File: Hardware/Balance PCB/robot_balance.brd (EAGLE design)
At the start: 100 x 50 mm, 47 parts, among them Q1 16Mhz

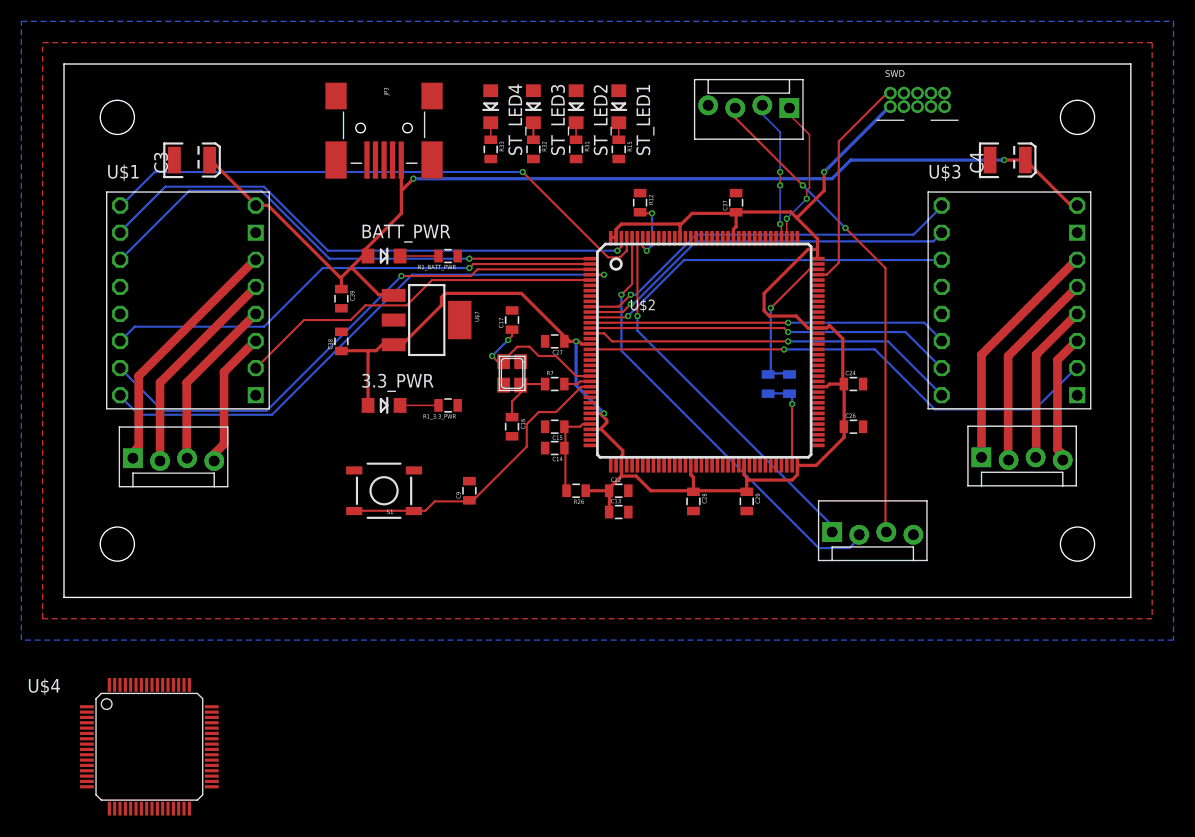
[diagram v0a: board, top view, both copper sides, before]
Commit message: Replaced 144 pin Balancing MCU with smaller 64 pin version and added a .gitignore file
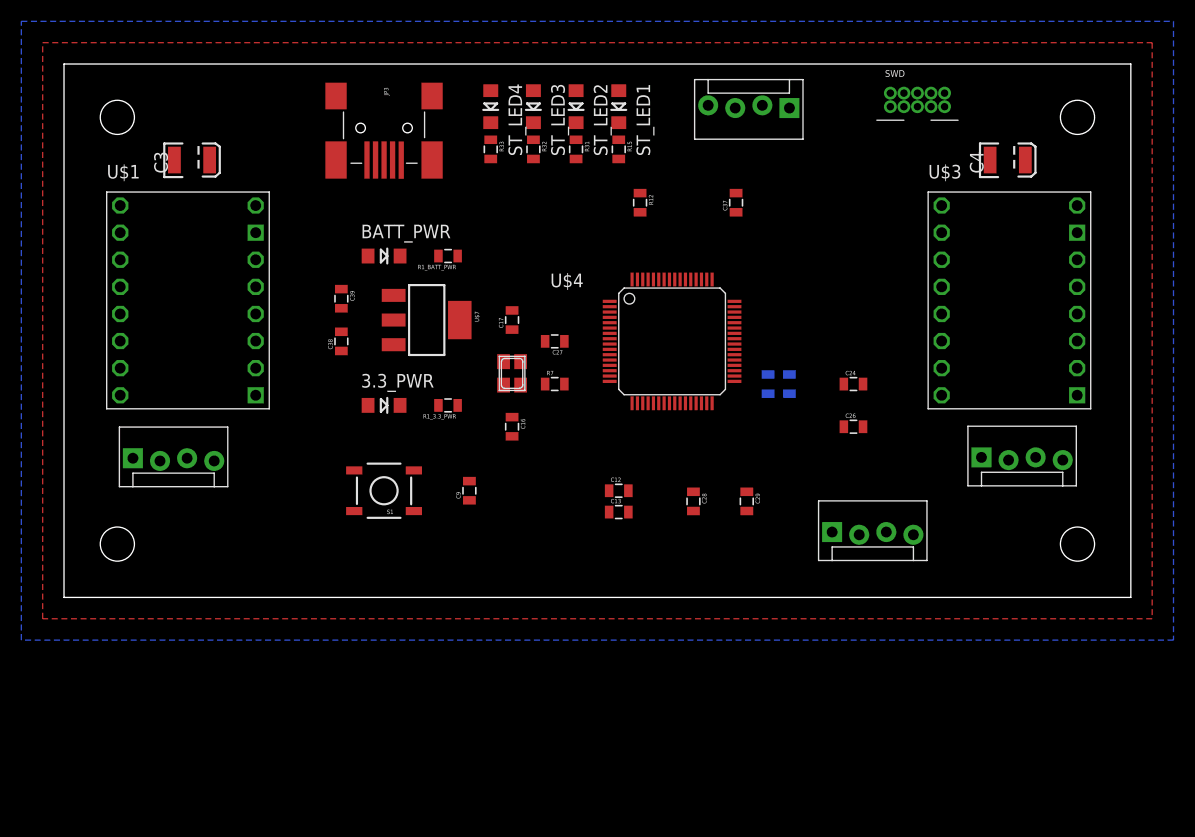
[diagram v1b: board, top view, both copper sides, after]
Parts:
- removed C14: 0.1uF, SparkFun-Capacitors:0805
- removed C15: 1uF, SparkFun-Capacitors:0805
- removed R26: 47, SparkFun-Passives:0805
- removed U$2: STM32F407ZG, CAMERA:LQFP-144-20X20MM
- moved U$4 62.0 mm to (57.0, 24.0)
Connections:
- removed net N$10: C9.1, S1.1, S1.2, U$2.25
- removed net N$11: R12.2, U$2.138
- removed net N$14: C14.1, C15.1, R26.2, U$2.32
- removed net N$15: C17.1, Q1.3, U$2.23
- removed net N$22: R7.2, U$2.24
- removed net N$42: ST_LED1.A, U$2.127
- removed net N$44: ST_LED2.A, U$2.128
- removed net N$46: ST_LED3.A, U$2.129
- removed net N$48: ST_LED4.A, U$2.132
- removed net NRST: U$4.7
- removed net VCAP_1: U$4.31
- removed net VCAP_2: U$4.47
- removed net VDDA: U$4.13
- removed net VDD_1: U$4.32
- removed net VDD_2: U$4.48
- removed net VDD_3: U$4.64
- removed net VDD_4: U$4.19
- removed net VSSA: U$4.12
- removed net VSS_3: U$4.63
- removed net VSS_4: U$4.18
- new net !RST: C9.1, S1.1, S1.2, U$4.7
- new net BOOOT0: R12.2
- new net LED1: ST_LED1.A, U$4.53
- new net LED2: ST_LED2.A, U$4.2
- new net LED3: ST_LED3.A, U$4.3
- new net LED4: ST_LED4.A, U$4.4
- new net OSC_IN: C17.1, Q1.3, U$4.5
- new net OSC_OUT: R7.2, U$4.6
- net !S1_ENABLE: now also U$4.14; no longer U$2.141
- net !S1_FAULT: now also U$4.22; no longer U$2.5
- net !S1_SLEEP: now also U$4.17; no longer U$2.2
- net !S2_ENABLE: now also U$4.26; no longer U$2.10
- net !S2_FAULT: now also U$4.58; no longer U$2.18
- net !S2_SLEEP: now also U$4.55; no longer U$2.13
- net 3.3V: now also U$4.13, U$4.19, U$4.32, U$4.48, U$4.64; no longer R26.1, U$2.108, U$2.121, U$2.131, U$2.143, U$2.144, U$2.17, U$2.30, U$2.33, U$2.39, U$2.52, U$2.62, U$2.72, U$2.84, U$2.95
- net ARDUINO_RX: now also U$4.52; no longer U$2.112
- net ARDUINO_TX: now also U$4.51; no longer U$2.111
- net GND: now also U$4.12, U$4.18, U$4.63; no longer C14.2, C15.2, U$2.107, U$2.120, U$2.130, U$2.16, U$2.31, U$2.38, U$2.51, U$2.61, U$2.83, U$2.94
- net IMU_SCL: now also U$4.61; no longer U$2.139
- net IMU_SDA: now also U$4.62; no longer U$2.140
- net N$12: now also U$4.47; no longer U$2.106
- net N$2: now also U$4.31; no longer U$2.71
- net S1_DIR: now also U$4.21; no longer U$2.4
- net S1_M0: now also U$4.15; no longer U$2.142
- net S1_M1: now also U$4.16; no longer U$2.1
- net S1_STEP: now also U$4.20; no longer U$2.3
- net S2_DIR: now also U$4.57; no longer U$2.15
- net S2_M0: now also U$4.27; no longer U$2.11
- net S2_M1: now also U$4.28; no longer U$2.12
- net S2_STEP: now also U$4.56; no longer U$2.14
- net SWCLK: now also U$4.49; no longer U$2.109
- net SWDIO: now also U$4.46; no longer U$2.105
- net VBAT: no longer U$2.6
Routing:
- net 3.3V: track 157.1 -> 0.00 mm, vias 3 -> 0
- net V_USB: track 103.3 -> 0.00 mm, vias 2 -> 0
- net !S1_ENABLE: track 53.5 -> 0.00 mm, vias 1 -> 0
- net S1_DIR: track 52.9 -> 0.00 mm, vias 1 -> 0
- net S1_M0: track 52.3 -> 0.00 mm, vias 1 -> 0
- net S1_STEP: track 51.2 -> 0.00 mm, vias 1 -> 0
- net !S2_FAULT: track 49.5 -> 0.00 mm, vias 1 -> 0
- net S1_M1: track 49.4 -> 0.00 mm, vias 1 -> 0
- net !S1_SLEEP: track 47.1 -> 0.00 mm, vias 1 -> 0
- net V_BATT: track 45.6 -> 0.00 mm, vias 2 -> 0
- net IMU_SDA: track 41.6 -> 0.00 mm, vias 1 -> 0
- net !S2_ENABLE: track 36.9 -> 0.00 mm, vias 1 -> 0
- net S2_M0: track 36.0 -> 0.00 mm, vias 1 -> 0
- net S2_DIR: track 35.3 -> 0.00 mm, vias 1 -> 0
- net S2_M1: track 35.1 -> 0.00 mm, vias 1 -> 0
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
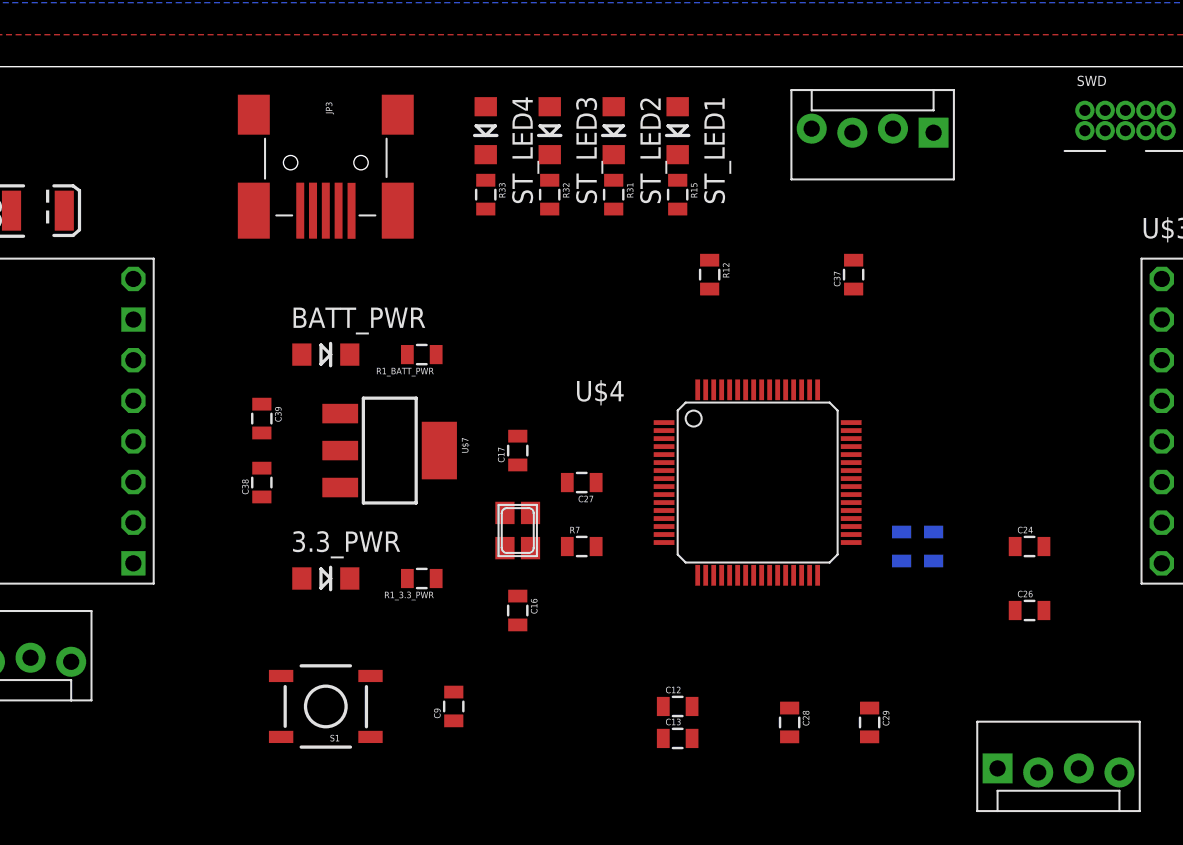
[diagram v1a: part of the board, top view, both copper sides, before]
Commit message: Added FTDI USB to Serial Converter as ALI suggested
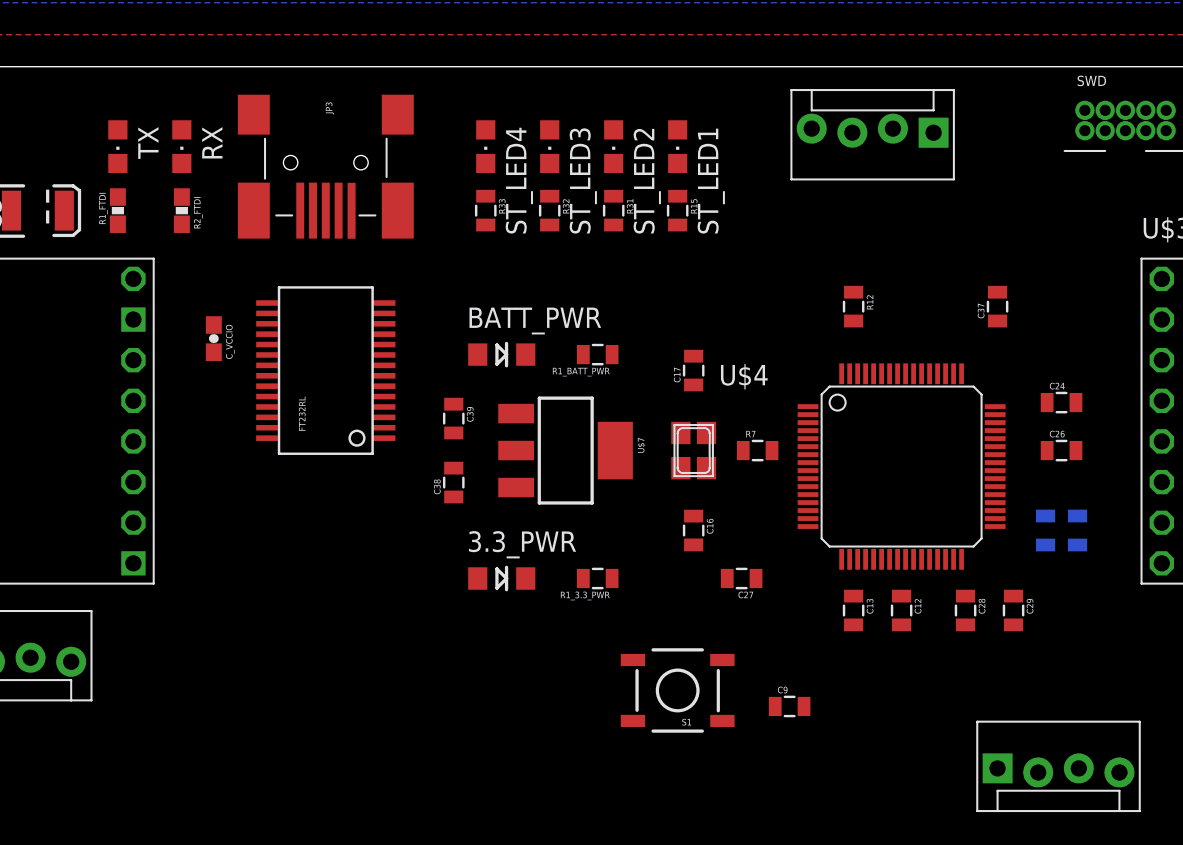
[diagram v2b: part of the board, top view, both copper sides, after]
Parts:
- added C_VCCIO: 0.1uF, SparkFun-Capacitors:0603-CAP
- added FT232RL: FT232RLSSOP, SparkFun-DigitalIC:SSOP28DB
- added R1_FTDI, R2_FTDI: 1K, SparkFun-Passives:0603-RES
- added RX, TX: (no value), adafruit:CHIPLED_0805
- ST_LED1, ST_LED2, ST_LED3, ST_LED4: device LilyPad-Wearables:LED-1206 -> adafruit:CHIPLED_0805
- moved S1 22.0 mm to (52.0, 11.0)
- moved C9 21.0 mm to (59.0, 10.0), turned to 0 degrees
- moved C12 15.2 mm to (66.0, 16.0), turned to 270 degrees
- moved C13 13.6 mm to (63.0, 16.0), turned to 270 degrees
- moved C28 13.0 mm to (70.0, 16.0)
- moved R7 12.5 mm to (57.0, 26.0)
- moved C16 12.1 mm to (53.0, 21.0)
- moved C17 12.1 mm to (53.0, 31.0)
- moved Q1 12.1 mm to (53.0, 26.0)
- moved C38 12.0 mm to (38.0, 24.0)
- moved C39 12.0 mm to (38.0, 28.0)
- moved C27 11.7 mm to (56.0, 18.0)
- moved C29 11.4 mm to (73.0, 16.0)
- moved 3.3_PWR 11.0 mm to (41.0, 18.0)
- moved BATT_PWR 11.0 mm to (41.0, 32.0)
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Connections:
- removed net V_BATT: JP4.3, JP5.3
- new net 5V: BATT_PWR.A, C39.1, FT232RL.20, JP3.VBUS, JP4.3, JP5.3, RX.A, TX.A, U$7.1
- new net BOOT0: U$4.60
- new net N$10: FT232RL.22, R2_FTDI.2
- new net N$11: R2_FTDI.1, RX.C
- new net N$13: C_VCCIO.1, FT232RL.17, FT232RL.4
- new net N$8: FT232RL.23, R1_FTDI.1
- new net N$9: R1_FTDI.2, TX.C
- new net UART3_RX: FT232RL.1, U$4.30
- new net UART3_TX: FT232RL.5, U$4.29
- new net USB_D+: FT232RL.15, JP3.D+
- new net USB_D-: FT232RL.16, JP3.D-
- net GND: now also C_VCCIO.2, FT232RL.18, FT232RL.21, FT232RL.25, FT232RL.26, FT232RL.7; no longer JP3.1, JP3.2, JP3.3, JP3.4
- net V_USB: no longer BATT_PWR.A, C39.1, JP3.VBUS, U$7.1

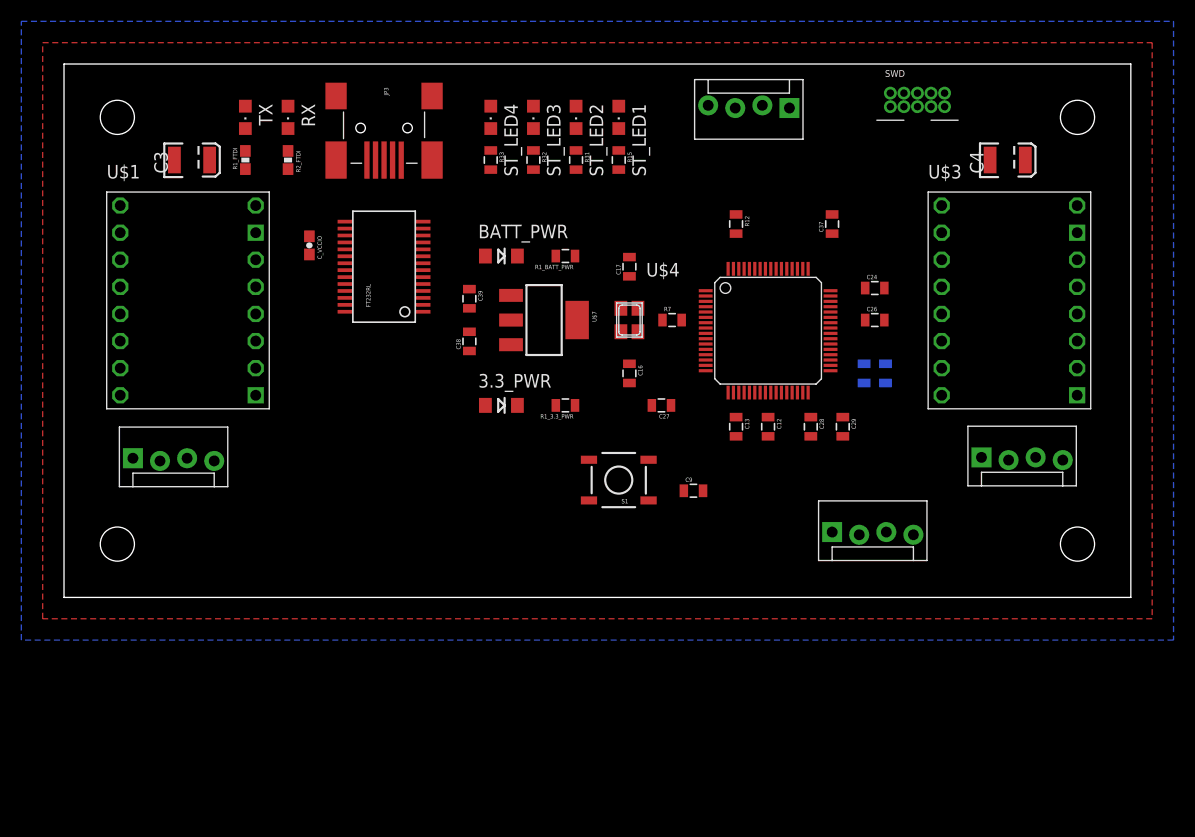
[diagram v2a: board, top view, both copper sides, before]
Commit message: Put a larger JTAG connector
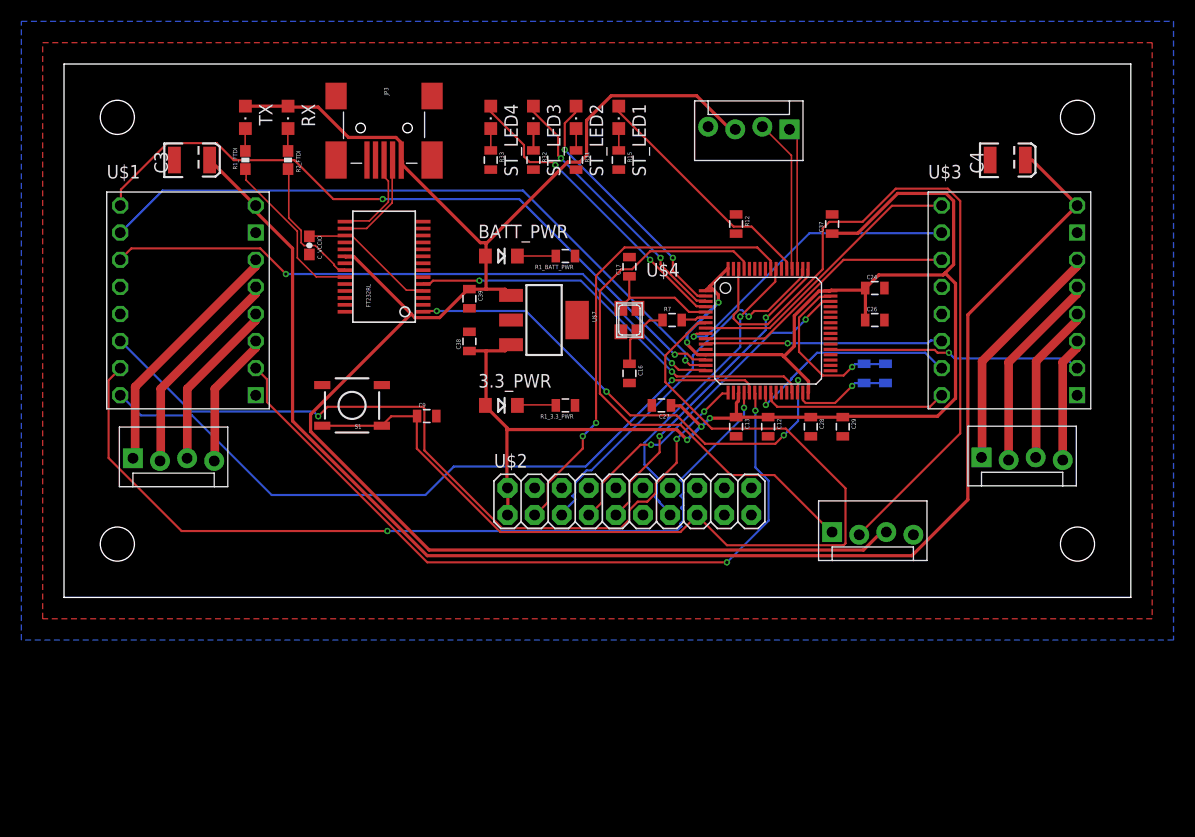
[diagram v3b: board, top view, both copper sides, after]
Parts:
- removed SWD: (no value), Sandwich:JTAG-10-1.27MM
- added U$2: JTAG_20PIN, JonathanLukas:2X10
- moved C9 26.0 mm to (34.0, 17.0)
- moved S1 26.0 mm to (27.0, 18.0)
- moved JP4 2.00 mm to (68.0, 44.0)
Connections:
- removed net VBAT: U$4.1
- new net !JTRST: U$2.3, U$4.56
- new net JTDI: U$2.5, U$4.50
- net !RST: now also U$2.15
- net !S2_ENABLE: now also U$4.8; no longer U$4.26
- net !S2_FAULT: now also U$4.37; no longer U$4.58
- net !S2_SLEEP: now also U$4.11; no longer U$4.55
- net 3.3V: now also U$2.1, U$2.2, U$4.1; no longer SWD.1
- net GND: now also U$2.10, U$2.12, U$2.14, U$2.16, U$2.18, U$2.20, U$2.4, U$2.6, U$2.8; no longer SWD.3, SWD.5, SWD.9
- net S2_DIR: now also U$4.25; no longer U$4.57
- net S2_M0: now also U$4.9; no longer U$4.27
- net S2_M1: now also U$4.10; no longer U$4.28
- net S2_STEP: now also U$4.24; no longer U$4.56
- net SWCLK: now also U$2.9; no longer SWD.4
- net SWDIO: now also U$2.7; no longer SWD.2
- net SWO: now also U$2.13, U$4.55; no longer SWD.6
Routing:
- net 5V: track 0.00 -> 159.2 mm
- net 3.3V: track 0.00 -> 150.0 mm, vias 0 -> 5
- net V_USB: track 0.00 -> 136.9 mm
- net !RST: track 0.00 -> 91.4 mm
- net S1_STEP: track 0.00 -> 81.2 mm, vias 0 -> 2
- net !S1_SLEEP: track 0.00 -> 74.9 mm, vias 0 -> 3
- net !S1_FAULT: track 0.00 -> 71.0 mm, vias 0 -> 2
- net IMU_SDA: track 0.00 -> 69.5 mm
- net S1_DIR: track 0.00 -> 68.3 mm, vias 0 -> 1
- net !S1_ENABLE: track 0.00 -> 66.6 mm, vias 0 -> 2
- net S1_M0: track 0.00 -> 63.7 mm, vias 0 -> 1
- net S1_M1: track 0.00 -> 60.1 mm, vias 0 -> 2
- net IMU_SCL: track 0.00 -> 52.9 mm
- net UART3_RX: track 0.00 -> 46.3 mm, vias 0 -> 4
- net !JTRST: track 0.00 -> 43.6 mm, vias 0 -> 2
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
